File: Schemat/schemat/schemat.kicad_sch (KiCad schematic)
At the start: 17 parts, among them Q1 BC327, SW1 SW_DIP_x01

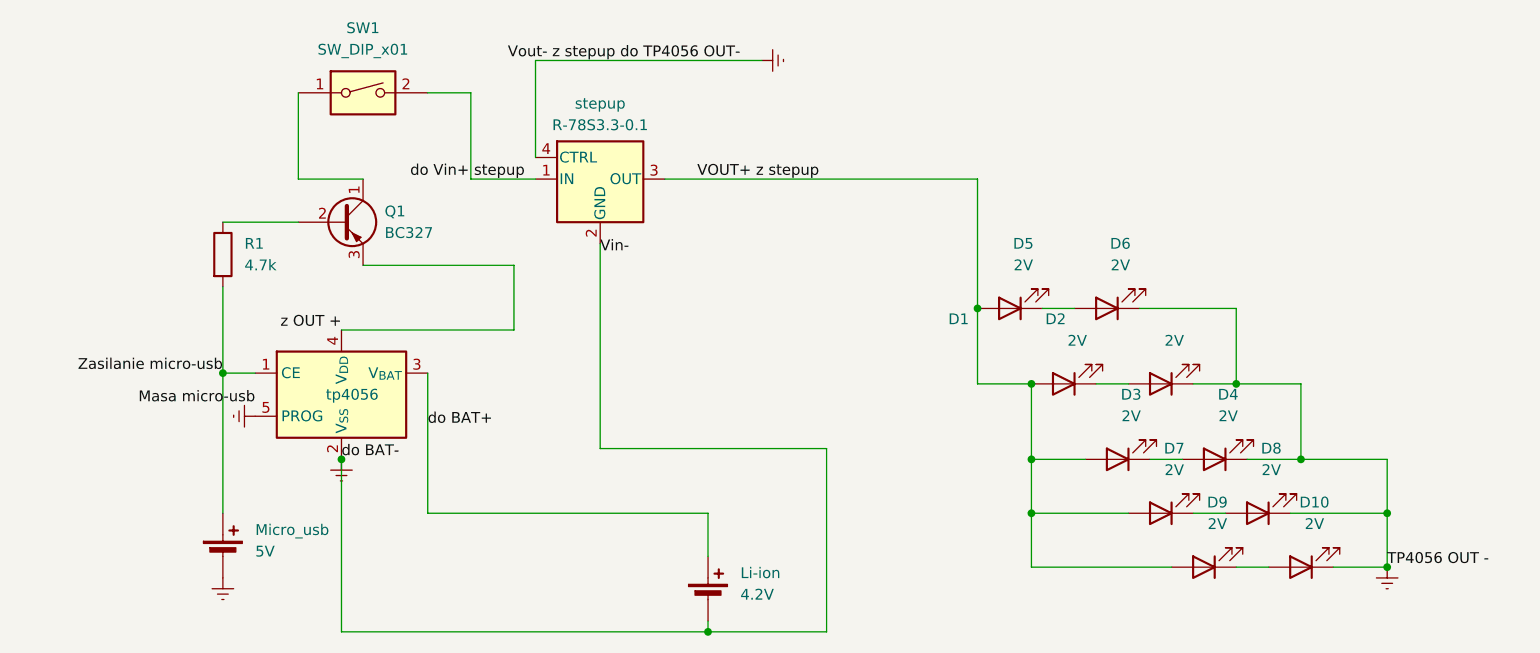
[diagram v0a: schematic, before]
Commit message: własne symbole, zmieniony in- przetwornicy
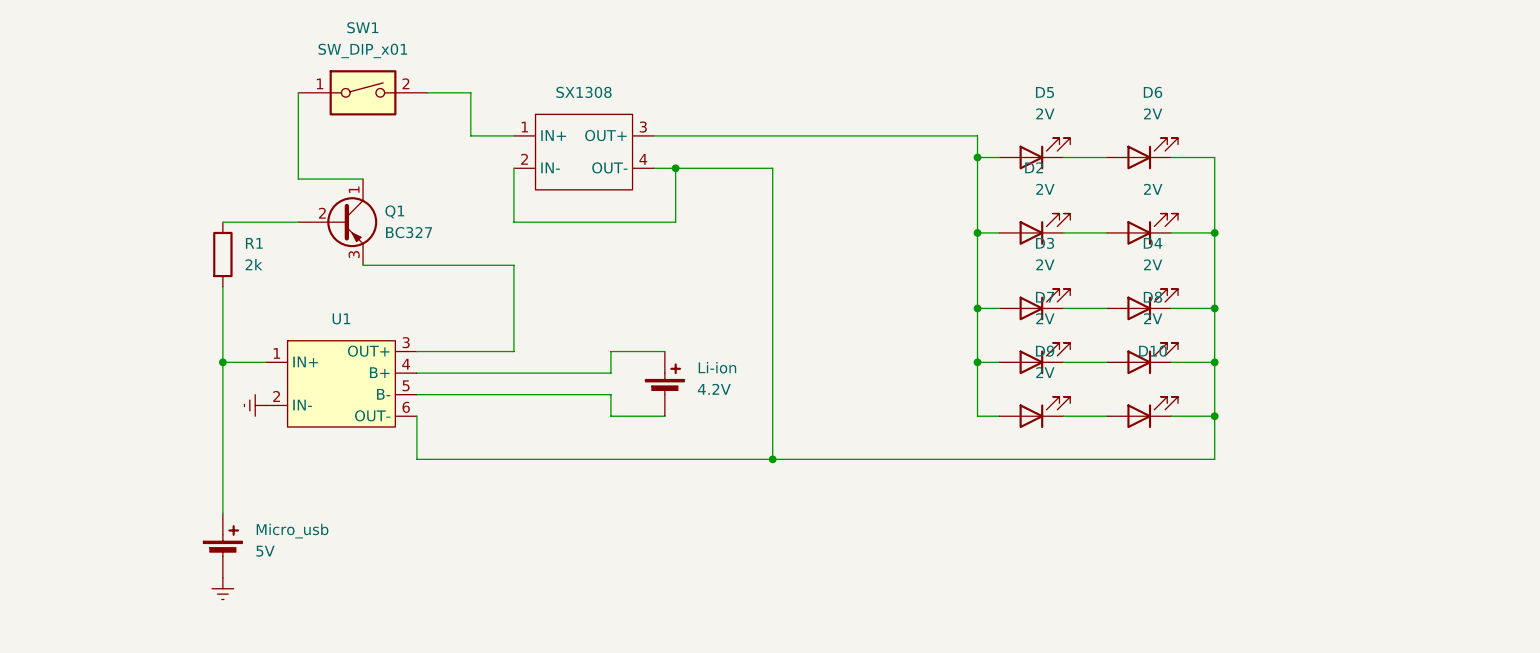
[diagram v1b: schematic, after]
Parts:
- removed stepup: R-78S3.3-0.1, Converter_DCDC:Converter_DCDC_RECOM_R-78S-0.1_THT, symbol Regulator_Switching:R-78S3.3-0.1
- removed tp4056: MCP73811T-420I-OT, Package_TO_SOT_SMD:SOT-23-5, symbol Battery_Management:MCP73811T-420I-OT
- added SX1308: ~, symbol step-up:SX1308
- added U1: ~, symbol tp4056:TP4056_bufor
- R1: value 4.7k -> 2k
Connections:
- net Earth: now also U1.2 (IN-); no longer D10.1 (K), D2.1 (K), D4.1 (K), D6.1 (K), D8.1 (K), Li-ion.2 (-)
- net VOUT+ z stepup: no longer names the net of D1.2 (A), D3.2 (A), D5.2 (A), D7.2 (A), D9.2 (A)
- net VOUT+ z stepup: now also SX1308.3 (OUT+)
- net Zasilanie micro-usb: no longer names the net of Micro_usb.1 (+), R1.2
- net Zasilanie micro-usb: now also U1.1 (IN+)
- net do BAT+: no longer names the net of Li-ion.1 (+)
- net do BAT+: now also U1.4 (B+)
- net do Vin+ stepup: no longer names the net of SW1.2
- net do Vin+ stepup: now also SX1308.1 (IN+)
- net z OUT +: no longer names the net of Q1.3 (E)
- net z OUT +: now also U1.3 (OUT+)
- new net: D10.1 (K), D2.1 (K), D4.1 (K), D6.1 (K), D8.1 (K), SX1308.2 (IN-), SX1308.4 (OUT-), U1.6 (OUT-)
- new net: Li-ion.2 (-), U1.5 (B-)
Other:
- moved on the sheet: D10, D2, D3, D4, D5, D6, D7, D8, D9, Li-ion
